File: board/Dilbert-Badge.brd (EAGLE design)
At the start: 106.7 x 52.1 mm, 46 parts, among them IC1 MCP23017SO, J1 IO EXP., J2 FTDI_DEVICE, J3 NEOPIXEL, J4 PWR IN, J5 I2C, SW1 UP, SW2 DOWN, SW3 LEFT, SW4 RIGHT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

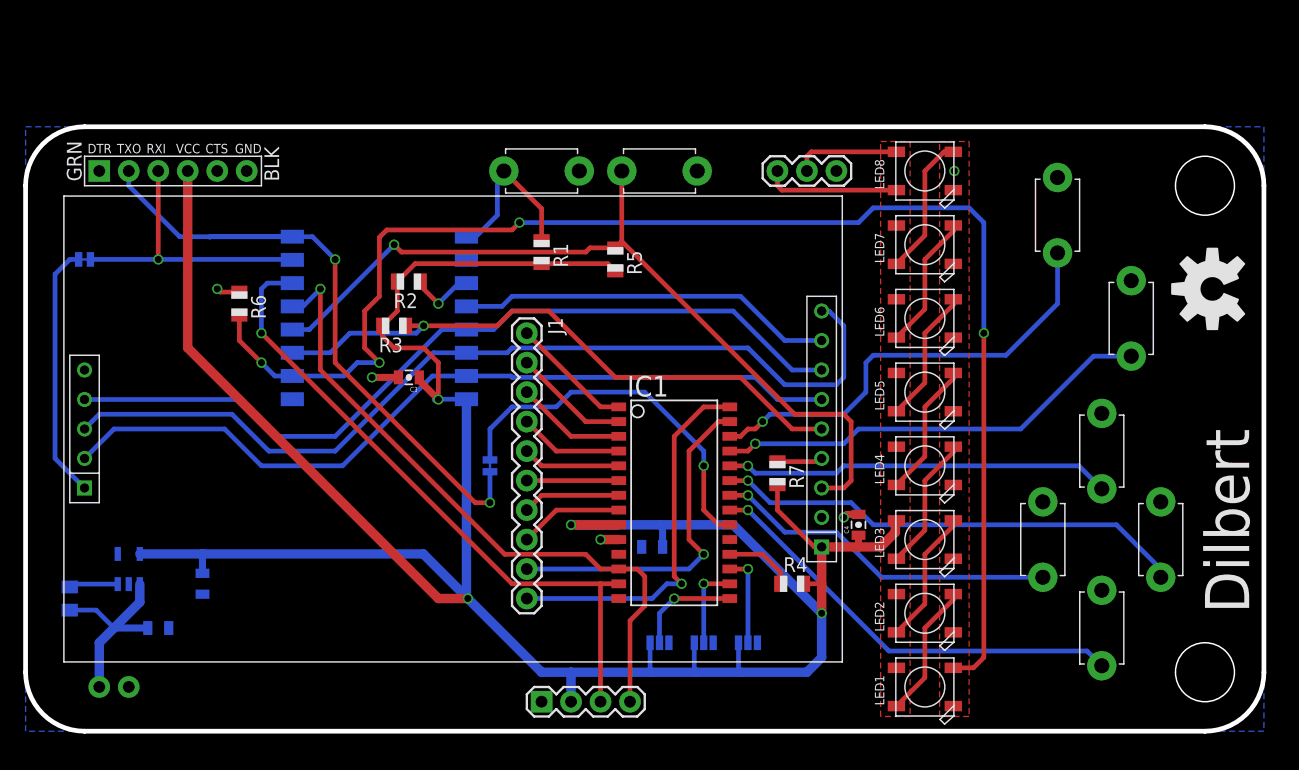
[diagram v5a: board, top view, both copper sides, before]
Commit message: clean up text, maximise gropund plane width
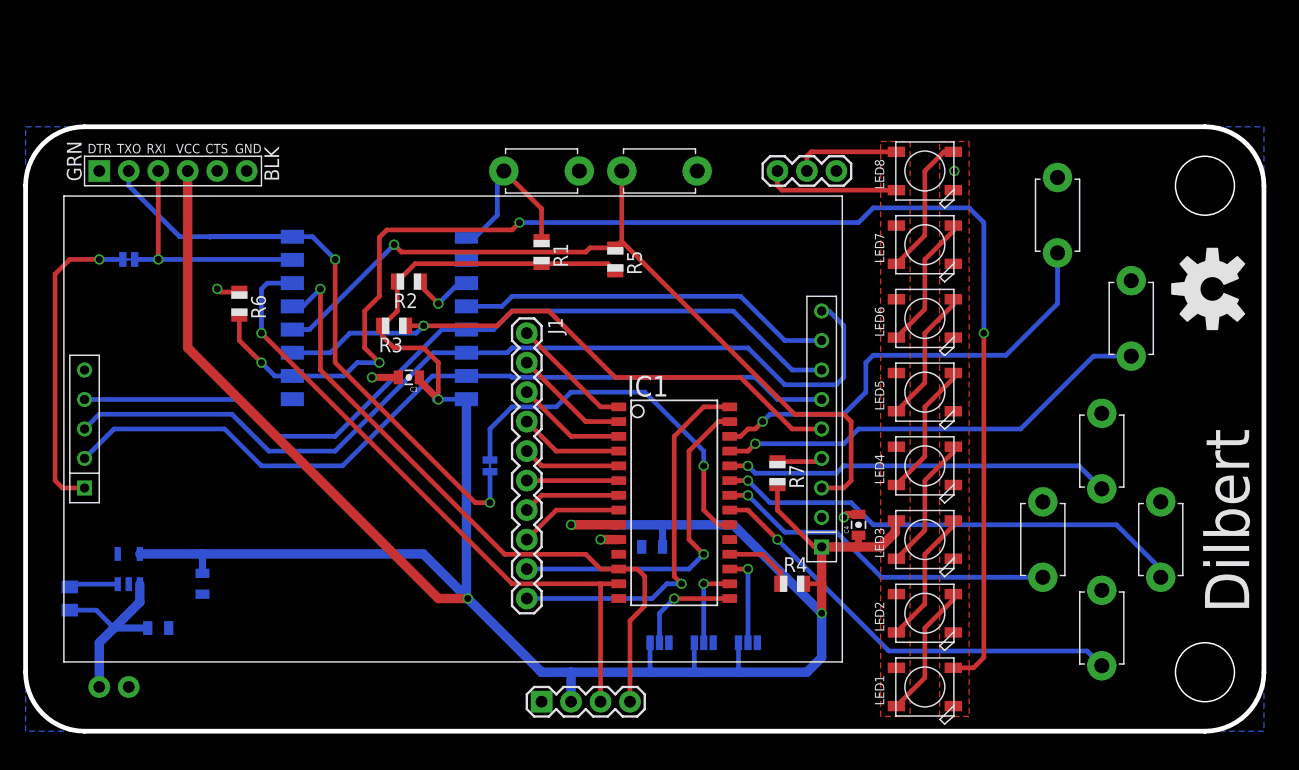
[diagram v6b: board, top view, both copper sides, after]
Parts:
- moved JP5 3.81 mm to (6.35, 45.7)
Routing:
- net SD_CS: track 22.0 -> 27.0 mm, vias 0 -> 1
- net UART_RX: track 25.0 -> 21.2 mm
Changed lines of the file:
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@@
 <layer number="28" name="bValues" color="7" fill="1" visible="yes" active="yes"/>
 <layer number="29" name="tStop" color="7" fill="3" visible="no" active="yes"/>
-<layer number="30" name="bStop" color="7" fill="6" visible="no" active="yes"/>
+<layer number="30" name="bStop" color="7" fill="6" visible="yes" active="yes"/>
 <layer number="31" name="tCream" color="7" fill="4" visible="no" active="yes"/>
 <layer number="32" name="bCream" color="7" fill="5" visible="no" active="yes"/>
@@
 <text x="6.35" y="10.795" size="1.016" layer="28" rot="MR90" align="center-left">GND</text>
 <text x="3.81" y="10.795" size="1.016" layer="28" rot="MR90" align="center-left">VIN</text>
+<rectangle x1="19.05" y1="48.895" x2="36.83" y2="56.515" layer="42"/>
 </plain>
 <attributes>
@@
 <element name="X1" library="adafruit" package="ESP-12" value="" x="27.94" y="43.18" rot="MR0"/>
 <element name="SW1" library="adafruit" package="TACT_PANA-EVQ" value="UP" x="85.09" y="21.59" smashed="yes" rot="R270">
-<attribute name="VALUE" x="82.639" y="24.606" size="0.4064" layer="27" ratio="10" rot="R270"/>
+<attribute name="VALUE" x="82.004" y="24.606" size="0.8128" layer="27" ratio="10" rot="R270"/>
 </element>
 <element name="SW2" library="adafruit" package="TACT_PANA-EVQ" value="DOWN" x="95.25" y="21.59" smashed="yes" rot="R270">
-<attribute name="VALUE" x="92.799" y="24.606" size="0.4064" layer="27" ratio="10" rot="R270"/>
+<attribute name="VALUE" x="92.164" y="24.606" size="0.8128" layer="27" ratio="10" rot="R270"/>
 </element>
 <element name="SW3" library="adafruit" package="TACT_PANA-EVQ" value="LEFT" x="90.17" y="29.21" smashed="yes" rot="R270">
-<attribute name="VALUE" x="87.719" y="32.226" size="0.4064" layer="27" ratio="10" rot="R270"/>
+<attribute name="VALUE" x="87.084" y="32.226" size="0.8128" layer="27" ratio="10" rot="R270"/>
 </element>
 <element name="SW4" library="adafruit" package="TACT_PANA-EVQ" value="RIGHT" x="90.17" y="13.97" smashed="yes" rot="R270">
-<attribute name="VALUE" x="87.719" y="16.986" size="0.4064" layer="27" ratio="10" rot="R270"/>
+<attribute name="VALUE" x="87.084" y="16.986" size="0.8128" layer="27" ratio="10" rot="R270"/>
 </element>
 <element name="SW5" library="adafruit" package="TACT_PANA-EVQ" value="A" x="92.71" y="40.64" smashed="yes" rot="R270">
-<attribute name="VALUE" x="90.259" y="43.656" size="0.4064" layer="27" ratio="10" rot="R270"/>
+<attribute name="VALUE" x="87.719" y="43.656" size="2.54" layer="27" ratio="10" rot="R270"/>
 </element>
 <element name="SW6" library="adafruit" package="TACT_PANA-EVQ" value="B" x="86.36" y="49.53" smashed="yes" rot="R270">
-<attribute name="VALUE" x="83.909" y="52.546" size="0.4064" layer="27" ratio="10" rot="R270"/>
+<attribute name="VALUE" x="81.369" y="52.546" size="2.54" layer="27" ratio="10" rot="R270"/>
 </element>
 <element name="SW7" library="adafruit" package="TACT_PANA-EVQ" value="RESET" x="41.91" y="53.34" smashed="yes" rot="R180">
-<attribute name="VALUE" x="44.926" y="55.791" size="0.4064" layer="27" ratio="10" rot="R180"/>
+<attribute name="VALUE" x="44.926" y="56.426" size="0.8128" layer="27" ratio="10" rot="R180"/>
 </element>
 <element name="IC1" library="adafruit" package="SO28W" value="MCP23017SO" x="53.34" y="25.4" rot="R270"/>
 <element name="SW8" library="adafruit" package="TACT_PANA-EVQ" value="SWD" x="52.07" y="53.34" smashed="yes" rot="R180">
-<attribute name="VALUE" x="55.086" y="55.791" size="0.4064" layer="27" ratio="10" rot="R180"/>
+<attribute name="VALUE" x="55.086" y="56.426" size="0.8128" layer="27" ratio="10" rot="R180"/>
 </element>
 <element name="LOGO1" library="SparkFun-Aesthetics" package="OSHW-LOGO-L" value="OSHW-LOGOL" x="99.695" y="43.18" rot="R90"/>
@@
 <element name="JP3" library="SparkFun-Passives" package="PAD-JUMPER-3-NO_YES_SILK" value="MCP IO A2" x="59.69" y="12.7" rot="MR0"/>
 <element name="JP4" library="SparkFun-Passives" package="PAD-JUMPER-2-NC_BY_TRACE_NO_SILK" value="IO INT TO UART TX" x="37.465" y="27.94" rot="MR90"/>
-<element name="JP5" library="SparkFun-Passives" package="PAD-JUMPER-2-NC_BY_TRACE_NO_SILK" value="SD CS TO UART RX" x="2.54" y="45.72" rot="MR0"/>
+<element name="JP5" library="SparkFun-Passives" package="PAD-JUMPER-2-NC_BY_TRACE_NO_SILK" value="SD CS TO UART RX" x="6.35" y="45.72" rot="MR0"/>
 <element name="U$2" library="mechanical" package="5MM_HOLE" value="5MM_MOUNTING_HOLE" x="99.06" y="10.16"/>
 <element name="U$3" library="mechanical" package="5MM_HOLE" value="5MM_MOUNTING_HOLE" x="99.06" y="52.07"/>
@@
 <signal name="BTN_R">
 <contactref element="SW4" pad="P$2"/>
-<wire x1="71.83" y1="11.99" x2="59.69" y2="24.13" width="0.4064" layer="16"/>
 <wire x1="71.83" y1="11.99" x2="88.9" y2="11.99" width="0.4064" layer="16"/>
 <wire x1="88.9" y1="11.99" x2="90.17" y2="10.72" width="0.4064" layer="16"/>
 <contactref element="IC1" pad="21"/>
 <wire x1="58.12" y1="24.13" x2="59.69" y2="24.13" width="0.4064" layer="1"/>
-<via x="59.69" y="24.13" extent="1-16" drill="0.6"/>
+<wire x1="59.69" y1="24.13" x2="62.23" y2="21.59" width="0.4064" layer="1"/>
+<via x="62.23" y="21.59" extent="1-16" drill="0.6"/>
+<wire x1="62.23" y1="21.59" x2="71.83" y2="11.99" width="0.4064" layer="16"/>
 </signal>
 <signal name="BTN_A">
@@
 <contactref element="J2" pad="P$3"/>
 <contactref element="JP5" pad="1"/>
-<wire x1="3.048" y1="45.72" x2="8.89" y2="45.72" width="0.4064" layer="16"/>
 <wire x1="8.89" y1="45.72" x2="20.4" y2="45.72" width="0.4064" layer="16"/>
 <wire x1="20.4" y1="45.72" x2="20.44" y2="45.68" width="0.4064" layer="16"/>
 <wire x1="8.89" y1="53.34" x2="8.89" y2="45.72" width="0.4064" layer="1"/>
 <via x="8.89" y="45.72" extent="1-16" drill="0.6"/>
+<wire x1="6.858" y1="45.72" x2="8.89" y2="45.72" width="0.4064" layer="16"/>
 </signal>
 <signal name="NEOPIXEL_OUT">
@@
 <contactref element="U$1" pad="SD_CS"/>
 <contactref element="JP5" pad="2"/>
-<wire x1="2.032" y1="45.72" x2="1.27" y2="45.72" width="0.4064" layer="16"/>
-<wire x1="1.27" y1="45.72" x2="0" y2="44.45" width="0.4064" layer="16"/>
-<wire x1="0" y1="44.45" x2="0" y2="28.575" width="0.4064" layer="16"/>
-<wire x1="0" y1="28.575" x2="2.54" y2="26.035" width="0.4064" layer="16"/>
+<wire x1="0" y1="44.45" x2="0" y2="26.67" width="0.4064" layer="1"/>
+<wire x1="2.54" y1="26.035" x2="0.635" y2="26.035" width="0.4064" layer="1"/>
+<wire x1="0.635" y1="26.035" x2="0" y2="26.67" width="0.4064" layer="1"/>
+<wire x1="5.842" y1="45.72" x2="3.81" y2="45.72" width="0.4064" layer="16"/>
+<via x="3.81" y="45.72" extent="1-16" drill="0.6"/>
+<wire x1="3.81" y1="45.72" x2="1.27" y2="45.72" width="0.4064" layer="1"/>
+<wire x1="1.27" y1="45.72" x2="0" y2="44.45" width="0.4064" layer="1"/>
 </signal>
 <signal name="N$4">

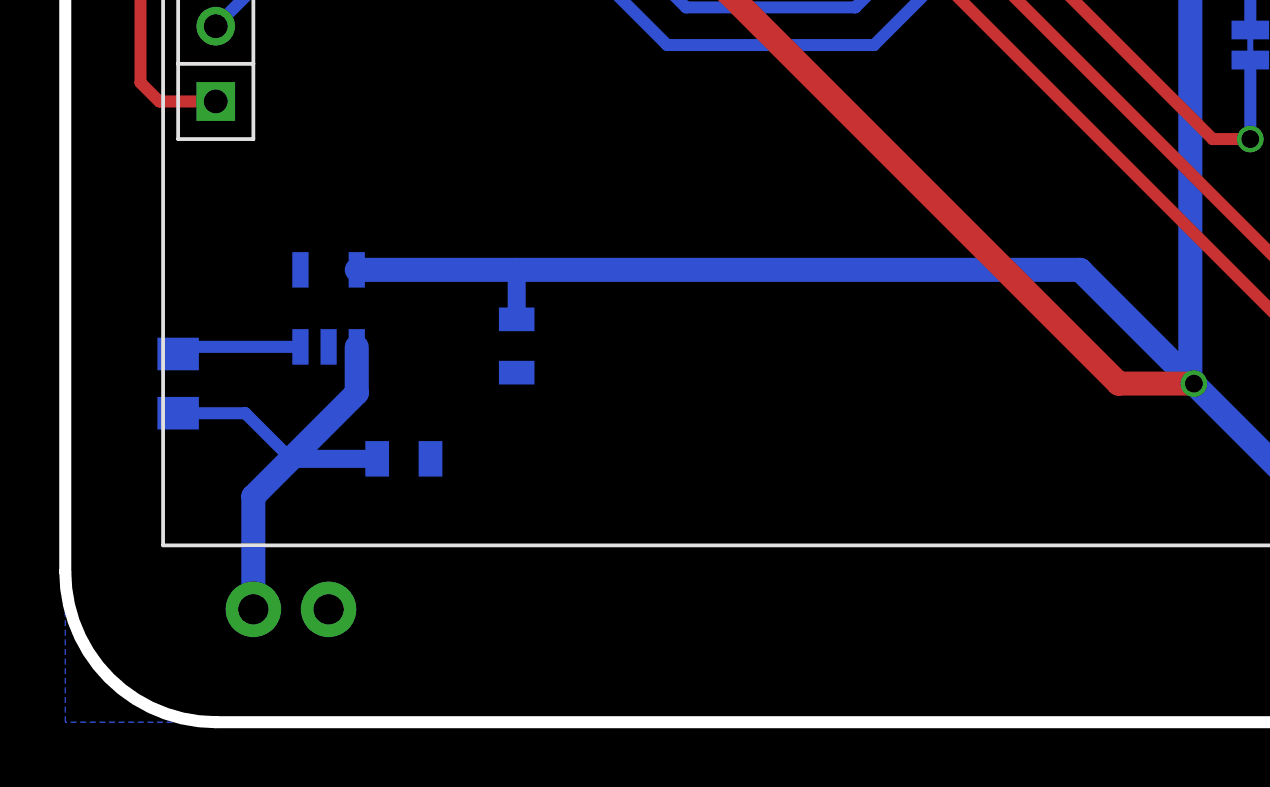
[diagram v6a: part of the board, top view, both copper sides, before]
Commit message: add hole for landscape lanyard
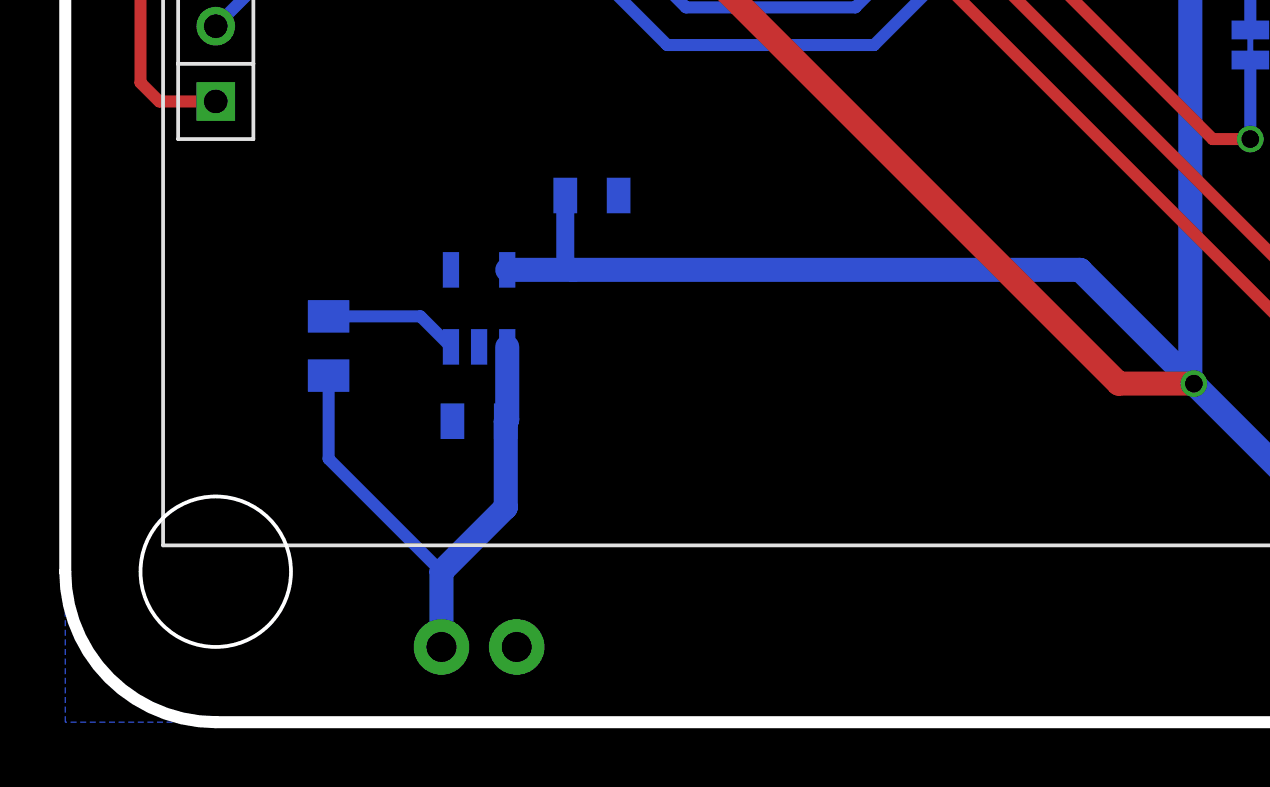
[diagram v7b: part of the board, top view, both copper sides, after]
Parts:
- added U$4: 5MM_MOUNTING_HOLE, mechanical:5MM_HOLE
- moved J4 6.48 mm to (12.7, 7.62)
- moved C2 5.68 mm to (15.2, 22.9), turned to 180 degrees
- moved R8 5.24 mm to (6.35, 17.8)
- moved U1 5.08 mm to (11.4, 19.1)
- moved C1 2.84 mm to (11.4, 15.2), turned to 0 degrees
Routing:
- net 3V3: track 247.5 -> 243.4 mm
- net VIN: track 17.7 -> 19.2 mm
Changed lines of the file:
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@@
 <text x="49.53" y="9.525" size="1.27" layer="28" rot="MR90" align="center-left">SCL</text>
 <text x="46.99" y="9.525" size="1.27" layer="28" rot="MR90" align="center-left">SDA</text>
-<text x="6.35" y="10.795" size="1.016" layer="28" rot="MR90" align="center-left">GND</text>
-<text x="3.81" y="10.795" size="1.016" layer="28" rot="MR90" align="center-left">VIN</text>
+<text x="12.7" y="9.525" size="1.016" layer="28" rot="MR90" align="center-left">GND</text>
+<text x="10.16" y="9.525" size="1.016" layer="28" rot="MR90" align="center-left">VIN</text>
 <rectangle x1="19.05" y1="48.895" x2="36.83" y2="56.515" layer="42"/>
 </plain>
@@
 <attribute name="VALUE" x="60.96" y="56.515" size="1.27" layer="28" rot="MR180"/>
 </element>
-<element name="U1" library="SparkFun-PowerIC" package="SOT23-5" value="3.3V" x="6.35" y="19.05" rot="MR0">
-<attribute name="PROD_ID" value="VREG-12457" x="6.35" y="19.05" size="1.778" layer="28" rot="MR0" display="off"/>
-</element>
-<element name="J4" library="SparkFun-Connectors" package="1X02" value="PWR IN" x="6.35" y="8.89" smashed="yes" rot="MR0">
-<attribute name="VALUE" x="15.24" y="8.255" size="1.27" layer="28" rot="MR0"/>
-</element>
-<element name="R8" library="adafruit" package="R0805" value="1K" x="1.27" y="16.51" rot="MR270"/>
-<element name="C1" library="SparkFun-Capacitors" package="0805-CAP" value="1.0uF" x="8.89" y="13.97" rot="MR180">
-<attribute name="PROD_ID" value="CAP-11625" x="8.89" y="13.97" size="1.016" layer="28" rot="MR180" display="off"/>
-</element>
-<element name="C2" library="SparkFun-Capacitors" package="0805-CAP" value="1.0uF" x="12.7" y="17.78" rot="MR270">
-<attribute name="PROD_ID" value="CAP-11625" x="12.7" y="17.78" size="1.016" layer="28" rot="MR270" display="off"/>
+<element name="U1" library="SparkFun-PowerIC" package="SOT23-5" value="3.3V" x="11.43" y="19.05" rot="MR0">
+<attribute name="PROD_ID" value="VREG-12457" x="11.43" y="19.05" size="1.778" layer="28" rot="MR0" display="off"/>
+</element>
+<element name="J4" library="SparkFun-Connectors" package="1X02" value="PWR IN" x="12.7" y="7.62" smashed="yes" rot="MR0">
+<attribute name="VALUE" x="21.59" y="6.985" size="1.27" layer="28" rot="MR0"/>
+</element>
+<element name="R8" library="adafruit" package="R0805" value="1K" x="6.35" y="17.78" rot="MR270"/>
+<element name="C1" library="SparkFun-Capacitors" package="0805-CAP" value="1.0uF" x="11.43" y="15.24" rot="MR0">
+<attribute name="PROD_ID" value="CAP-11625" x="11.43" y="15.24" size="1.016" layer="28" rot="MR0" display="off"/>
+</element>
+<element name="C2" library="SparkFun-Capacitors" package="0805-CAP" value="1.0uF" x="15.24" y="22.86" rot="MR180">
+<attribute name="PROD_ID" value="CAP-11625" x="15.24" y="22.86" size="1.016" layer="28" rot="MR180" display="off"/>
 </element>
 <element name="C3" library="SparkFun-Capacitors" package="0805-CAP" value="1.0uF" x="30.48" y="35.56" rot="R180">
@@
 <attribute name="PROD_ID" value="CAP-11625" x="55.245" y="26.035" size="1.016" layer="28" rot="MR0" display="off"/>
 </element>
+<element name="U$4" library="mechanical" package="5MM_HOLE" value="5MM_MOUNTING_HOLE" x="2.54" y="10.16"/>
 </elements>
 <signals>
@@
 <wire x1="29.48" y1="41.275" x2="28.21" y2="40.005" width="0.4064" layer="1"/>
 <contactref element="U1" pad="5"/>
-<wire x1="7.3" y1="20.3501" x2="12.7" y2="20.3501" width="0.8128" layer="16"/>
-<wire x1="12.7" y1="20.3501" x2="31.7199" y2="20.3501" width="0.8128" layer="16"/>
 <wire x1="31.7199" y1="20.3501" x2="35.56" y2="16.51" width="0.8128" layer="16"/>
 <contactref element="C2" pad="1"/>
@@
 <contactref element="C4" pad="1"/>
 <contactref element="C5" pad="1"/>
-<wire x1="12.7" y1="18.68" x2="12.7" y2="20.3501" width="0.6096" layer="16"/>
 <wire x1="33.02" y1="33.655" x2="32.755" y2="33.655" width="0.6096" layer="16"/>
 <wire x1="28.21" y1="40.005" x2="28.21" y2="39.1" width="0.4064" layer="1"/>
@@
 <wire x1="52.335" y1="20.955" x2="52.335" y2="22.595" width="0.6096" layer="16"/>
 <wire x1="52.335" y1="22.595" x2="52.07" y2="22.86" width="0.6096" layer="16"/>
+<wire x1="31.7199" y1="20.3501" x2="14.605" y2="20.3501" width="0.8128" layer="16"/>
+<wire x1="14.605" y1="20.3501" x2="12.38" y2="20.3501" width="0.8128" layer="16"/>
+<wire x1="14.34" y1="22.86" x2="14.34" y2="20.6151" width="0.6096" layer="16"/>
+<wire x1="14.34" y1="20.6151" x2="14.605" y2="20.3501" width="0.6096" layer="16"/>
 <wire x1="72.48" y1="48.64" x2="72.48" y2="54.99" width="0" layer="19" extent="1-1"/>
 </signal>
@@
 <contactref element="R8" pad="2"/>
 <contactref element="C1" pad="1"/>
-<wire x1="7.3" y1="17.7499" x2="7.3" y2="16.19" width="0.8128" layer="16"/>
-<wire x1="7.3" y1="16.19" x2="5.08" y2="13.97" width="0.8128" layer="16"/>
-<wire x1="5.08" y1="13.97" x2="3.81" y2="12.7" width="0.8128" layer="16"/>
-<wire x1="3.81" y1="12.7" x2="3.81" y2="8.89" width="0.8128" layer="16"/>
-<wire x1="7.99" y1="13.97" x2="5.08" y2="13.97" width="0.6096" layer="16"/>
-<wire x1="1.27" y1="15.51" x2="3.54" y2="15.51" width="0.4064" layer="16"/>
-<wire x1="3.54" y1="15.51" x2="5.08" y2="13.97" width="0.4064" layer="16"/>
+<wire x1="12.33" y1="15.24" x2="12.33" y2="12.33" width="0.8128" layer="16"/>
+<wire x1="12.33" y1="12.33" x2="10.16" y2="10.16" width="0.8128" layer="16"/>
+<wire x1="10.16" y1="10.16" x2="10.16" y2="7.62" width="0.8128" layer="16"/>
+<wire x1="12.38" y1="17.7499" x2="12.38" y2="15.29" width="0.8128" layer="16"/>
+<wire x1="12.38" y1="15.29" x2="12.33" y2="15.24" width="0.8128" layer="16"/>
+<wire x1="6.35" y1="16.78" x2="6.35" y2="13.97" width="0.4064" layer="16"/>
+<wire x1="6.35" y1="13.97" x2="10.16" y2="10.16" width="0.4064" layer="16"/>
 </signal>
 <signal name="VREG_EN">
 <contactref element="U1" pad="3"/>
 <contactref element="R8" pad="1"/>
-<wire x1="5.4" y1="17.7499" x2="1.5099" y2="17.7499" width="0.4064" layer="16"/>
-<wire x1="1.5099" y1="17.7499" x2="1.27" y2="17.51" width="0.4064" layer="16"/>
+<wire x1="6.35" y1="18.78" x2="9.4499" y2="18.78" width="0.4064" layer="16"/>
+<wire x1="9.4499" y1="18.78" x2="10.48" y2="17.7499" width="0.4064" layer="16"/>
 </signal>
 </signals>
